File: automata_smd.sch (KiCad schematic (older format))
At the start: 102 parts, among them J1 Barrel_Jack, J2 LCD, J3 ICSP, J4 SERIAL, Q1 2N2907, Q2 DMP2022LSS, SW1 INPUT_SEL, SW2 SW_DIP_x08, SW3 Reset, U1 4006, U10 TLC555, U11 TLC555, U12 4017, U13 74AHC1G04, U14 74AHC1G32, U15 74HC157, U16 74HC4040, U17 74HC11, U18 74HC11, U19 MC14557B, U2 74AHC1G86, U20 MC14557B, U21 4013, U22 4013, U23 ATmega328P-AU, U24 AMS1117-3.3, U3 74AHC1G86, U4 74AHC1G04, U5 74HC164, U6 TC40H373, U7 TC40H373, U8 4512, U9 74HC165, X1 16MHz

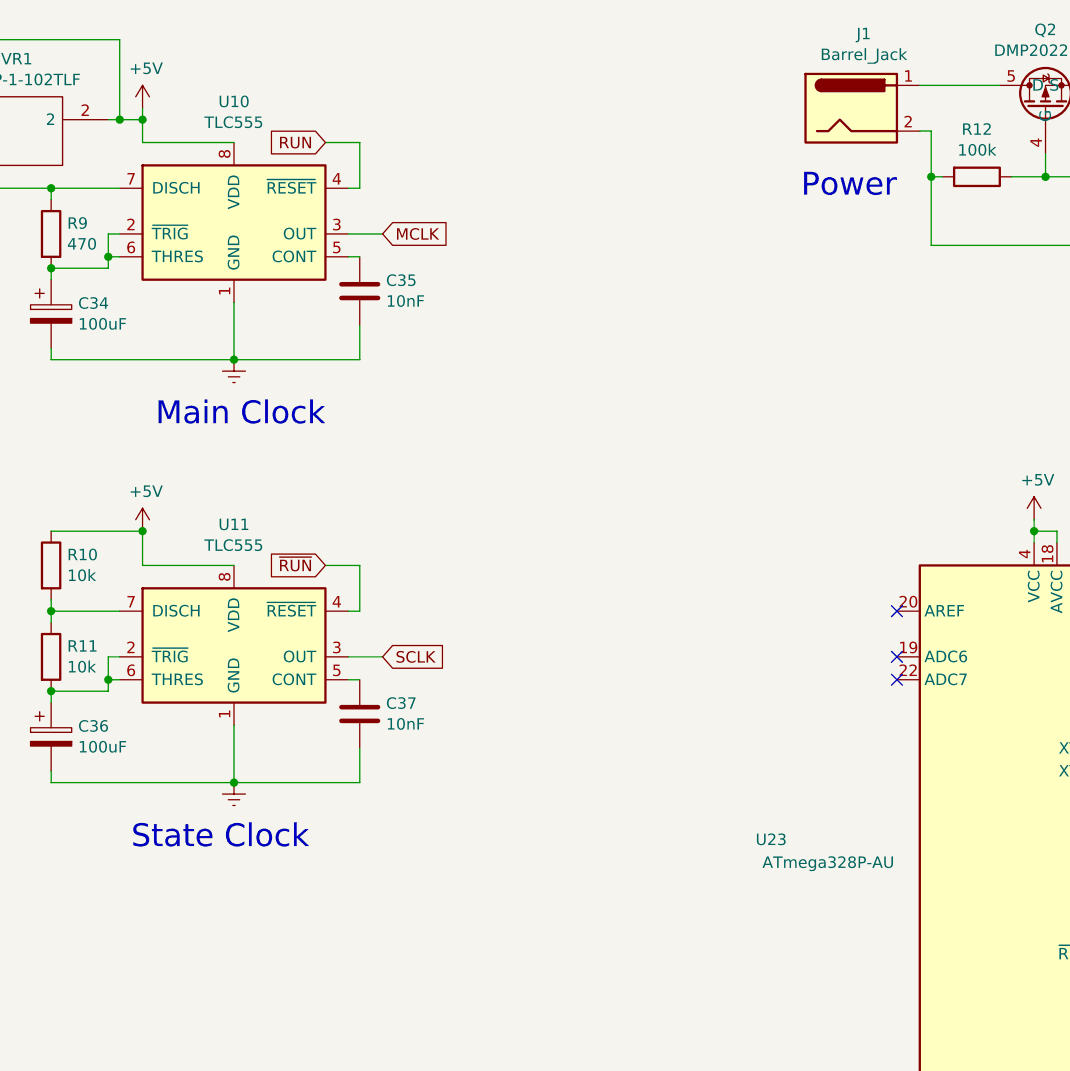
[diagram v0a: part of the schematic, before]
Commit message: Remove rescue libs and fixed MC14557 symbol error
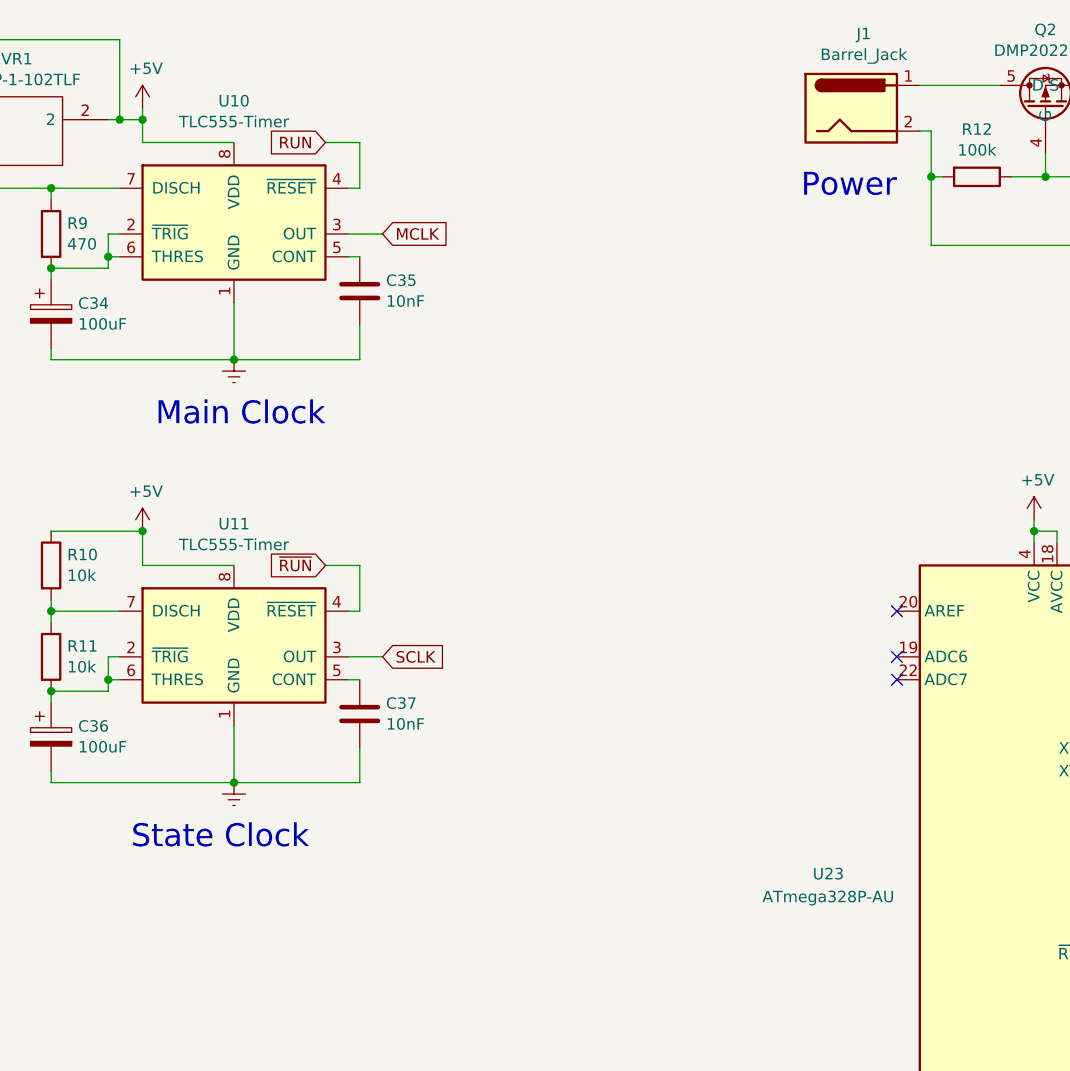
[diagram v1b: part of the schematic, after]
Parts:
- removed U10, U11: TLC555, Housings_SOIC:SOIC-8_3.9x4.9mm_Pitch1.27mm, symbol Timer:TLC555
- added U10, U11: TLC555-Timer, Package_SO:SOIC-8_3.9x4.9mm_P1.27mm, symbol automata_ic:TLC555-Timer
- U19, U20: footprint Housings_SOIC:SOIC-16W_7.5x10.3mm_Pitch1.27mm -> Package_SO:SOIC-16W_7.5x10.3mm_P1.27mm
- U23: footprint Housings_QFP:TQFP-32_7x7mm_Pitch0.8mm -> Package_QFP:TQFP-32_7x7mm_P0.8mm
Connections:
- net +5V: now also U10.8 (VDD), U11.8 (VDD)
- net GNDREF: now also U10.1 (GND), U11.1 (GND)
- net MCLK: now also U10.3 (OUT)
- net RUN: now also U10.4 (~RESET)
- net SCLK: now also U11.3 (OUT)
- net ~RUN: now also U11.4 (~RESET)
- net at C34.1, R9.2: now also U10.2 (~TRIG), U10.6 (THRES)
- net at C35.1: now also U10.5 (CONT)
- net at R9.1, VR1.3: now also U10.7 (DISCH)
- net at R10.2, R11.1: now also U11.7 (DISCH)
- net at C36.1, R11.2: now also U11.2 (~TRIG), U11.6 (THRES)
- net at C37.1: now also U11.5 (CONT)
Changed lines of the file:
@@
 EESchema Schematic File Version 4
-LIBS:automata_smd-cache
 EELAYER 30 0
 EELAYER END
@@
 Wire Wire Line
 	13500 3550 13350 3550
-$Comp
-L Timer:TLC555 U11
-U 1 1 5FC28C3D
-P 12850 3550
-F 0 "U11" H 12850 4128 50  0000 C CNN
-F 1 "TLC555" H 12850 4037 50  0000 C CNN
-F 2 "Housings_SOIC:SOIC-8_3.9x4.9mm_Pitch1.27mm" H 12900 3300 50  0001 L CNN
-F 3 "http://www.ti.com/lit/ds/symlink/tlc555.pdf" H 13500 3000 50  0001 C CNN
-	1    12850 3550
-	1    0    0    -1
-$EndComp
 Wire Wire Line
 	13400 3150 13400 3350
@@
 Text GLabel 13250 1300 0    50   Input ~ 0
 RUN
-$Comp
-L Timer:TLC555 U10
-U 1 1 5DD13032
-P 12850 1700
-F 0 "U10" H 12850 2278 50  0000 C CNN
-F 1 "TLC555" H 12850 2187 50  0000 C CNN
-F 2 "Housings_SOIC:SOIC-8_3.9x4.9mm_Pitch1.27mm" H 12900 1450 50  0001 L CNN
-F 3 "http://www.ti.com/lit/ds/symlink/tlc555.pdf" H 13500 1150 50  0001 C CNN
-	1    12850 1700
-	1    0    0    -1
-$EndComp
 Text Notes 13250 2550 2    100  ~ 0
 Main Clock
@@
 Wire Wire Line
 	8300 7500 8000 7500
-$Comp
-L 74xGxx:74AHC1G04 U13
-U 1 1 634E9617
-P 6250 8500
-F 0 "U13" H 6500 8750 50  0000 C CNN
-F 1 "74AHC1G04" H 6500 8650 50  0000 C CNN
-F 2 "TO_SOT_Packages_SMD:SOT-23-5" H 6250 8500 50  0001 C CNN
-F 3 "http://www.ti.com/lit/sg/scyt129e/scyt129e.pdf" H 6250 8500 50  0001 C CNN
-	1    6250 8500
-	1    0    0    -1
-$EndComp
 Wire Wire Line
 	6500 8500 6700 8500
@@
 	6250 8350 6250 8400
 $Comp
-L automata_ic:MC14557B U19
-U 1 1 63E967B8
-P 2750 13150
-F 0 "U19" H 2750 14281 50  0000 C CNN
-F 1 "MC14557B" H 2750 14190 50  0000 C CNN
-F 2 "Housings_SOIC:SOIC-16W_7.5x10.3mm_Pitch1.27mm" H 2750 14350 50  0001 C CNN
-F 3 "" H 2750 14350 50  0001 C CNN
-	1    2750 13150
-	1    0    0    -1
-$EndComp
-$Comp
 L power:+5V #PWR0127
 U 1 1 64103BE1
@@
 NoConn ~ 3300 12600
 $Comp
-L automata_ic:MC14557B U20
-U 1 1 65159900
-P 6400 13150
-F 0 "U20" H 6400 14281 50  0000 C CNN
-F 1 "MC14557B" H 6400 14190 50  0000 C CNN
-F 2 "Housings_SOIC:SOIC-16W_7.5x10.3mm_Pitch1.27mm" H 6400 14350 50  0001 C CNN
-F 3 "" H 6400 14350 50  0001 C CNN
-	1    6400 13150
-	1    0    0    -1
-$EndComp
-$Comp
 L power:+5V #PWR0130
 U 1 1 6515990A
@@
 Wire Wire Line
 	3700 8350 3700 8400
-Wire Wire Line
-	6250 8600 6250 8650
 $Comp
 L Device:C C24
@@
 Wire Wire Line
 	20600 4600 20600 4650
-$Comp
-L MCU_Microchip_ATmega:ATmega328P-AU U23
-U 1 1 5F0B65FB
-P 16350 4550
-F 0 "U23" H 15200 4750 50  0000 C CNN
-F 1 "ATmega328P-AU" H 15450 4650 50  0000 C CNN
-F 2 "Housings_QFP:TQFP-32_7x7mm_Pitch0.8mm" H 16350 4550 50  0001 C CIN
-F 3 "http://ww1.microchip.com/downloads/en/DeviceDoc/ATmega328_P%20AVR%20MCU%20with%20picoPower%20Technology%20Data%20Sheet%2040001984A.pdf" H 16350 4550 50  0001 C CNN
-	1    16350 4550
-	1    0    0    -1
-$EndComp
 NoConn ~ 15750 3550
 NoConn ~ 15750 3650
@@
 Wire Wire Line
 	15850 1050 16200 1050
+$Comp
+L automata_ic:MC14557B U19
+U 1 1 5F215ED0
+P 2750 13150
+F 0 "U19" H 2750 14281 50  0000 C CNN
+F 1 "MC14557B" H 2750 14190 50  0000 C CNN
+F 2 "Package_SO:SOIC-16W_7.5x10.3mm_P1.27mm" H 2750 14350 50  0001 C CNN
+F 3 "https://www.onsemi.com/pub/Collateral/MC14557-D.PDF" H 2750 14350 50  0001 C CNN
+	1    2750 13150
+	1    0    0    -1
+$EndComp
+$Comp
+L automata_ic:MC14557B U20
+U 1 1 5F216B38
+P 6400 13150
+F 0 "U20" H 6400 14281 50  0000 C CNN
+F 1 "MC14557B" H 6400 14190 50  0000 C CNN
+F 2 "Package_SO:SOIC-16W_7.5x10.3mm_P1.27mm" H 6400 14350 50  0001 C CNN
+F 3 "https://www.onsemi.com/pub/Collateral/MC14557-D.PDF" H 6400 14350 50  0001 C CNN
+	1    6400 13150
+	1    0    0    -1
+$EndComp
+$Comp
+L MCU_Microchip_ATmega:ATmega328P-AU U23
+U 1 1 5F2A6FBD
+P 16350 4550
+F 0 "U23" H 15450 4600 50  0000 C CNN
+F 1 "ATmega328P-AU" H 15450 4500 50  0000 C CNN
+F 2 "Package_QFP:TQFP-32_7x7mm_P0.8mm" H 16350 4550 50  0001 C CIN
+F 3 "http://ww1.microchip.com/downloads/en/DeviceDoc/ATmega328_P%20AVR%20MCU%20with%20picoPower%20Technology%20Data%20Sheet%2040001984A.pdf" H 16350 4550 50  0001 C CNN
+	1    16350 4550
+	1    0    0    -1
+$EndComp
+$Comp
+L automata_ic:TLC555-Timer U10
+U 1 1 5F4505FA
+P 12850 1700
+F 0 "U10" H 12850 2281 50  0000 C CNN
+F 1 "TLC555-Timer" H 12850 2190 50  0000 C CNN
+F 2 "Package_SO:SOIC-8_3.9x4.9mm_P1.27mm" H 12900 1450 50  0001 L CNN
+F 3 "" H 13500 1150 50  0001 C CNN
+	1    12850 1700
+	1    0    0    -1
+$EndComp
+$Comp
+L automata_ic:TLC555-Timer U11
+U 1 1 5F451482
+P 12850 3550
+F 0 "U11" H 12850 4131 50  0000 C CNN
+F 1 "TLC555-Timer" H 12850 4040 50  0000 C CNN
+F 2 "Package_SO:SOIC-8_3.9x4.9mm_P1.27mm" H 12900 3300 50  0001 L CNN
+F 3 "" H 13500 3000 50  0001 C CNN
+	1    12850 3550
+	1    0    0    -1
+$EndComp
+Wire Wire Line
+	6250 8600 6250 8650
 Wire Bus Line
 	8600 1450 8600 3950
@@
 Wire Bus Line
 	8600 3950 8600 5300
+$Comp
+L 74xGxx:74AHC1G04 U13
+U 1 1 634E9617
+P 6250 8500
+F 0 "U13" H 6500 8750 50  0000 C CNN
+F 1 "74AHC1G04" H 6500 8650 50  0000 C CNN
+F 2 "TO_SOT_Packages_SMD:SOT-23-5" H 6250 8500 50  0001 C CNN
+F 3 "http://www.ti.com/lit/sg/scyt129e/scyt129e.pdf" H 6250 8500 50  0001 C CNN
+	1    6250 8500
+	1    0    0    -1
+$EndComp
 $EndSCHEMATC

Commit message: Rev 3 design update for SMD version
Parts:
- removed U1: 4006, Housings_DIP:DIP-14_W7.62mm_Socket, symbol automata_ic:4006
- removed U2: 74AHC1G86, TO_SOT_Packages_SMD:SOT-23-5, symbol 74xGxx:74AHC1G86
- removed VR1: 3362P-1-102TLF, SamacSys_Parts:3362P_1, symbol SamacSys_Parts:3362P-1-102TLF
- added RV1: 1K, SamacSys_Parts:3362P_1, symbol Device:R_POT
- added U1, U2: 74HC164, Package_SO:TSSOP-14_4.4x5mm_P0.65mm, symbol automata_ic:74HC164
- C1: footprint Capacitors_SMD:C_0603 -> Package_SO:TSSOP-14_4.4x5mm_P0.65mm
- C10, C11, C12, C13, C14, C15, C16, C17, C18, C19, C2, C20, C21, C22, C23, C24, C3, C32, C33, C35, C37, C4, C5, C6, C7, C8, C9: footprint Capacitors_SMD:C_0603 -> Capacitor_SMD:C_0603_1608Metric
- C28: value 1000uF -> 100uF; footprint Capacitors_THT:CP_Radial_D10.0mm_P5.00mm -> Capacitor_THT:CP_Radial_D8.0mm_P2.50mm
- C29, C30, C31: footprint Capacitors_THT:CP_Radial_D5.0mm_P2.00mm -> Capacitor_THT:CP_Radial_D5.0mm_P2.00mm
- C34, C36: footprint Capacitors_THT:CP_Radial_D6.3mm_P2.50mm -> Capacitor_THT:CP_Radial_D8.0mm_P2.50mm
- D1, D10, D11, D2, D3, D4, D5, D6, D7, D9: footprint LEDs:LED_0603 -> LED_SMD:LED_0603_1608Metric
- D8: footprint Diodes_SMD:D_MELF -> Diode_SMD:D_MiniMELF
- J1: footprint Connectors:BARREL_JACK -> Connector_BarrelJack:BarrelJack_Horizontal
- J2: footprint Pin_Headers:Pin_Header_Straight_1x08_Pitch2.54mm -> Connector_PinHeader_2.54mm:PinHeader_1x08_P2.54mm_Vertical
- J3: footprint Pin_Headers:Pin_Header_Straight_2x03_Pitch2.54mm -> Connector_PinHeader_2.54mm:PinHeader_2x03_P2.54mm_Vertical
- J4: footprint Pin_Headers:Pin_Header_Straight_2x01_Pitch2.54mm -> Connector_PinHeader_2.54mm:PinHeader_2x01_P2.54mm_Vertical
- Q1: footprint TO_SOT_Packages_SMD:SOT-23 -> Package_TO_SOT_SMD:SOT-23
- Q2: footprint Power_Integrations:SO-8 -> Package_SO:SO-8_3.9x4.9mm_P1.27mm
- R1, R10, R11, R12, R13, R14, R16, R2, R9: footprint Resistors_SMD:R_0603 -> Resistor_SMD:R_0603_1608Metric
- R15, R17, R18, R19, R3, R4, R5, R6, R7, R8: value 330 -> 4K7; footprint Resistors_SMD:R_0603 -> Resistor_SMD:R_0603_1608Metric
- R20, R21: value 330 -> 470; footprint Resistors_SMD:R_0603 -> Resistor_SMD:R_0603_1608Metric
- SW2: footprint Housings_DIP:DIP-16_W7.62mm_Socket -> Button_Switch_THT:SW_DIP_SPSTx08_Slide_9.78x22.5mm_W7.62mm_P2.54mm
- SW3: footprint Buttons_Switches_THT:SW_PUSH_6mm -> Button_Switch_THT:SW_PUSH_6mm
- U12, U15, U16, U8, U9: footprint Housings_SSOP:TSSOP-16_4.4x5mm_Pitch0.65mm -> Package_SO:TSSOP-16_4.4x5mm_P0.65mm
- U13, U14, U3, U4: footprint TO_SOT_Packages_SMD:SOT-23-5 -> Package_TO_SOT_SMD:SOT-23-5
- U17, U18, U21, U22, U5: footprint Housings_SSOP:TSSOP-14_4.4x5mm_Pitch0.65mm -> Package_SO:TSSOP-14_4.4x5mm_P0.65mm
- U24: footprint TO_SOT_Packages_SMD:SOT-223-3_TabPin2 -> Package_TO_SOT_SMD:SOT-223-3_TabPin2
- U6, U7: footprint Housings_SSOP:TSSOP-20_4.4x6.5mm_Pitch0.65mm -> Package_SO:TSSOP-20_4.4x6.5mm_P0.65mm
- X1: footprint Crystals:Crystal_SMD_5032-2pin_5.0x3.2mm -> Crystal:Crystal_SMD_5032-2Pin_5.0x3.2mm
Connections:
- net +5V: now also RV1.1, RV1.2, U1.14 (VCC), U1.9 (~MR), U2.14 (VCC), U2.9 (~MR)
- net GNDREF: now also U1.7 (GND), U2.7 (GND)
- net MCLK: now also U1.8 (CP), U2.8 (CP)
- net at U3.2: now also U5.12 (Q6), U6.17 (D6)
- net at U5.1 (DSA), U5.2 (DSB): now also U2.13 (Q7); no longer U3.4
- net at R9.1, U10.7 (DISCH): now also RV1.3
- net at U5.4 (Q1), U6.4 (D1): now also U3.1
- net at U4.2: now also U3.4
- net at U4.4: now also U1.1 (DSA), U1.2 (DSB); no longer U3.1
- new net: U1.13 (Q7), U2.1 (DSA), U2.2 (DSB)
- no-connect marks 30 -> 41
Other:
- note added: "18th and 23th bit tap"
- note added: "23-bit Shift Register"
- note added: "Compatible with NCE30P12S"
- moved on the sheet: U3, U5

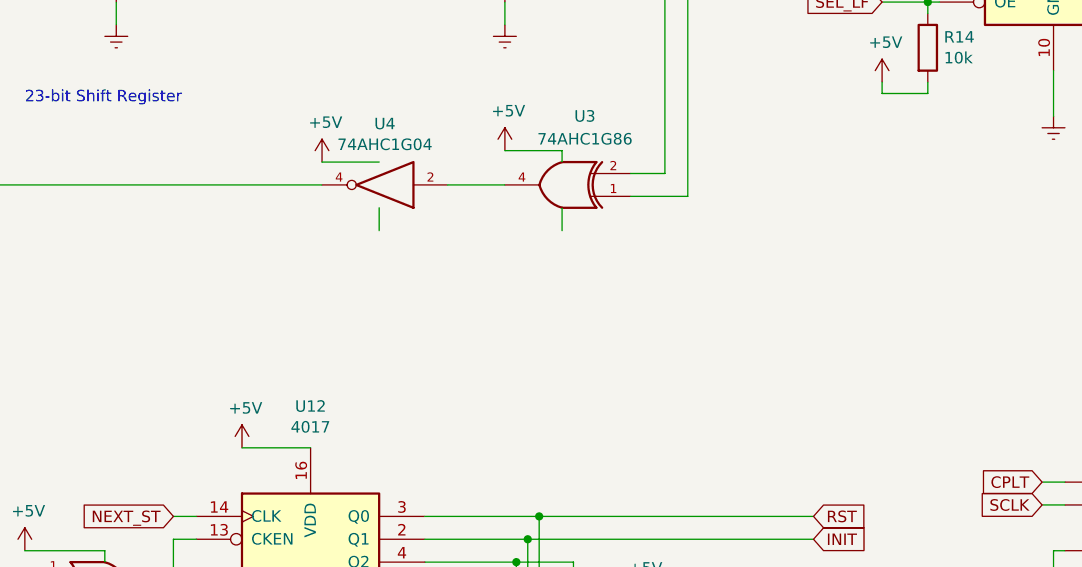
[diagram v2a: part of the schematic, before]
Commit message: PCB reroute
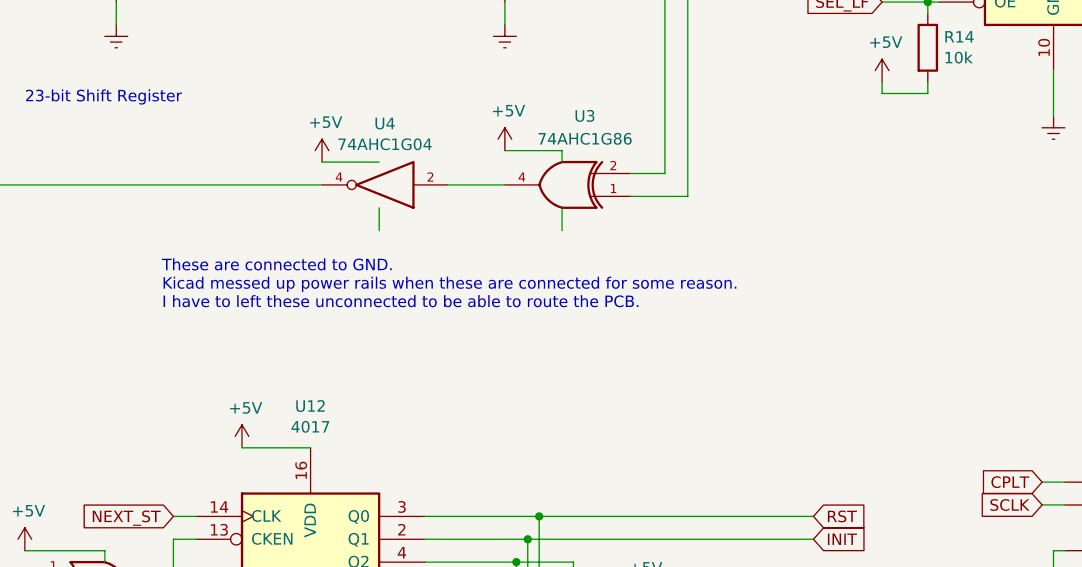
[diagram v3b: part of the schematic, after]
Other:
- note added: "These are connected to GND.\nKicad messed up power rails when these are connected for some reason.\nI have to left these unconnected to be able to route the PCB."
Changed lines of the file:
@@
 Wire Bus Line
 	8600 3950 8600 5300
+Text Notes 3850 7050 0    50   ~ 0
+These are connected to GND.\nKicad messed up power rails when these are connected for some reason.\nI have to left these unconnected to be able to route the PCB.
 $EndSCHEMATC
